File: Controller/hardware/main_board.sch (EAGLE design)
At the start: 45 parts, among them IC1 LINEAR_7805DT, IC2 40XX_4050D, IC3 ADAFRUIT_LP298XS, IC5 ATMEGA328, Q4 16MHZ, X1 ADAFRUIT_MICROSD, X4 CON-PHOENIX-508_MST2V

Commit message: added part numbers, consolidated parts,  cleaned up board/schematic
added part numbers for capacitors, resistors, ic's and the main 12v connector.

cleaned up the board layout a little, mainly just straightening traces.

fixed the through hole 100uf cap footprint to reflect the bom part, 2mm leads 5mm body

made both leds the same part number.

removed the polarized caps from the sd card and replaced with smd 0805 ceramic caps.

cleaned up the schematic a little and added a frame
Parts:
- 12V: device main_board:SPARKFUN_LED0805 -> main_board:LED_RED_08050805
- ACT: value RED -> ACT; device main_board:ADAFRUIT_LEDCHIP-LED0805 -> main_board:LED_RED_08050805
- C1: device main_board:10UF_08050805 -> main_board:C10UF_08050805
- C10, C4, C6, C7, C9: device main_board:100UF_ECE3.5-8 -> main_board:C100UF_ECE3.5-8
- C12, C13: device main_board:16PF_08050805 -> main_board:C16PF_08050805
- C14, C2, C3, C5, C8: device main_board:100NF_08050805 -> main_board:C0.1UF_08050805
- IC1: value LINEAR_7805DT -> LINEAR_78DT; device main_board:LINEAR_7805DT -> main_board:LINEAR_78DT
- IC3: value ADAFRUIT_LP298XS -> LP298XS; device main_board:ADAFRUIT_LP298XS -> main_board:LP298XS
- IC5: device main_board:SPARKFUN_ATMEGA168 -> main_board:ATMEGA328P
- R1: value 1K -> 1.0k; device main_board:ADAFRUIT_R-US_R0805 -> main_board:R1.0K_0805R0805
- R10: value 330r -> 330; device main_board:ADAFRUIT_R-US_R0805 -> main_board:R330_0805R0805
- R2, R3: value 10K -> 10k; device main_board:ADAFRUIT_R-US_R0805 -> main_board:R10K_0805R0805
- R7: value 10K -> 10k; device main_board:SPARKFUN_RESISTOR -> main_board:R10K_0805R0805
- R9: value 2.2K -> 2.2k; device main_board:SPARKFUN_RESISTOR -> main_board:R2.2K_0805R0805
- SW_NEXT: device main_board:ADAFRUIT_SPST_TACT-EVQQ2 -> main_board:TACT_SW_EVQQ2-EVQQ2
- X1: value ADAFRUIT_MICROSD -> MICROSD_SMD; device main_board:ADAFRUIT_MICROSD -> main_board:MICROSD_SMD
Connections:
- net +3V3: now also C2.1
- net VCC: no longer C2.1
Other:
- moved on the sheet: 12V, ACT, C1, C10, C12, C13, C14, C2, C3, C4, C5, C6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

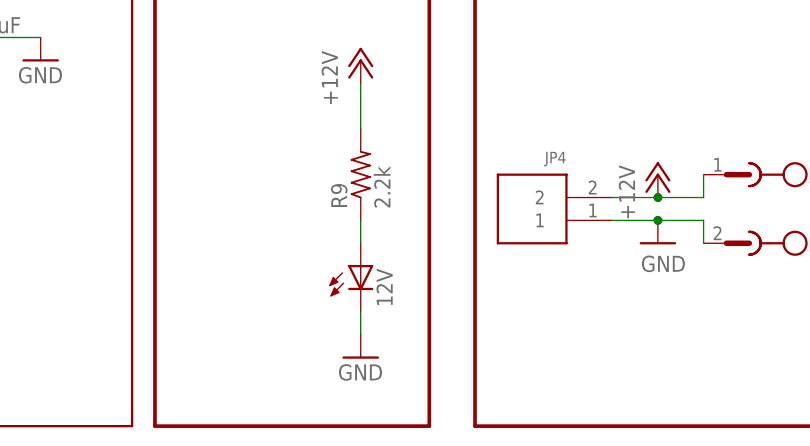
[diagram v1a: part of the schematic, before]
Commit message: final cleanup
little more silk screen shuffling and clearing DRC errors
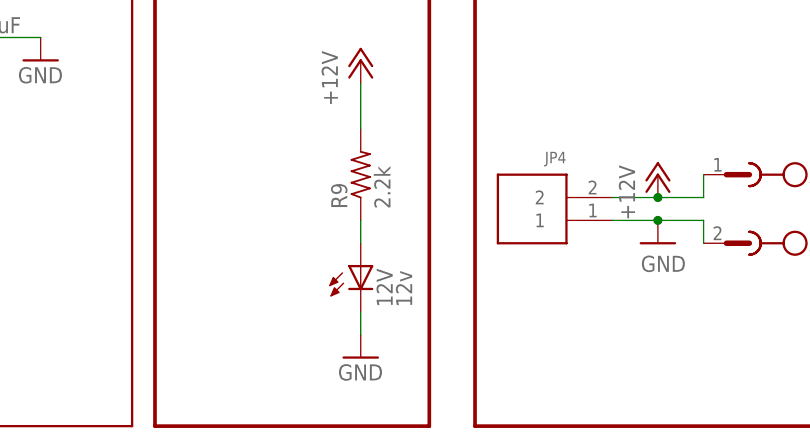
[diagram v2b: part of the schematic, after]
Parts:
- 12V: value (none) -> 12v
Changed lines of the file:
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@@
 <part name="P+18" library="main_board" deviceset="VCC" device=""/>
 <part name="R9" library="main_board" deviceset="R2.2K_0805" device="R0805" value="2.2k"/>
-<part name="12V" library="main_board" deviceset="LED_RED_0805" device="0805"/>
+<part name="12V" library="main_board" deviceset="LED_RED_0805" device="0805" value="12v"/>
 <part name="P+17" library="main_board" deviceset="+12V" device=""/>
 <part name="C8" library="main_board" deviceset="C0.1UF_0805" device="0805" value="0.1uF"/>
@@
 </sheet>
 </sheets>
-<errors>
-</errors>
 </schematic>
 </drawing>

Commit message: updated board name
changed board name to reflect copper changes
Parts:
- 12V: value 12v -> (none); device main_board:LED_RED_08050805 -> SparkFun:LED0805
- ACT: value ACT -> RED; device main_board:LED_RED_08050805 -> adafruit:LEDCHIP-LED0805
- C1: value 10uF -> 10uF/10V; device main_board:C10UF_08050805 -> adafruit:CPOL-USA/3216-18R
- C10, C4, C6, C7, C9: device main_board:C100UF_ECE3.5-8 -> rcl:CPOL-EUE3.5-8
- C12, C13: value 16pF -> 16pf; device main_board:C16PF_08050805 -> SparkFun:CAP0805
- C14, C3, C5, C8: value 0.1uF -> 100nF; device main_board:C0.1UF_08050805 -> SparkFun:CAP0805
- C2: device main_board:C0.1UF_08050805 -> adafruit:C-USC0805K
- IC1: value LINEAR_78DT -> 7805DT; device main_board:LINEAR_78DT -> linear:7805DT
- IC2: value 40XX_4050D -> 4050D; device main_board:40XX_4050D -> 40xx:4050D
- IC3: device main_board:LP298XS -> adafruit:LP298XS
- IC5: device main_board:ATMEGA328P -> SparkFun:ATMEGA168
- ICSP: device main_board:CON-HARTING-ML_ML6 -> con-harting-ml:ML6
- IC_A_MOTOR, IC_B_MOTOR: value POLOLU-STEPPER-DRIVER_2133-DRV8825 -> 2133-DRV8825; device main_board:POLOLU-STEPPER-DRIVER_2133-DRV8825 -> pololu-stepper-driver:2133-DRV8825
- J1: device main_board:JUMPER_J2X5MM -> jumper:J2X5MM
- JP1, JP5: device main_board:ADAFRUIT_PINHD-1X3 -> adafruit:PINHD-1X3
- JP4: value JST_EPH_2PIN -> 2PIN; device main_board:JST_EPH_2PIN -> jst_eph:2PIN
- MOTOR-A, MOTOR-B: value JST_EPH_4PIN -> 4PIN; device main_board:JST_EPH_4PIN -> jst_eph:4PIN
- Q4: device main_board:CRYSTAL_CRYSTALHC49S -> crystal:CRYSTALHC49S
- R1: value 1.0k -> 1K; device main_board:R1.0K_0805R0805 -> adafruit:R-US_R0805
- R10: value 330 -> 330r; device main_board:R330_0805R0805 -> adafruit:R-US_R0805
- R2, R3: value 10k -> 10K; device main_board:R10K_0805R0805 -> adafruit:R-US_R0805
- R7: value 10k -> 10K; device main_board:R10K_0805R0805 -> SparkFun:RESISTOR
- R9: value 2.2k -> 2.2K; device main_board:R2.2K_0805R0805 -> SparkFun:RESISTOR
- SJ1, SJ2, SJ3, SJ4, SJ5, SJ6: device main_board:JUMPER_SJ -> jumper:SJ
- SW_NEXT: device main_board:TACT_SW_EVQQ2-EVQQ2 -> adafruit:SPST_TACT-EVQQ2
- U$1: value DIY-MODULES_DISPLAY-OLED-128X64-I2C -> DISPLAY-OLED-128X64-I2C; device main_board:DIY-MODULES_DISPLAY-OLED-128X64-I2C -> diy-modules:DISPLAY-OLED-128X64-I2C
- X1: value MICROSD_SMD -> MICROSD; device main_board:MICROSD_SMD -> adafruit:MICROSD
- X4: value CON-PHOENIX-508_MST2V -> MST2V; device main_board:CON-PHOENIX-508_MST2V -> con-phoenix-508:MST2V
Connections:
- net +3V3: now also C1.+; no longer C1.1, C2.1
- net GND: now also C1.-; no longer C1.2
- net VCC: now also C2.1
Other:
- moved on the sheet: 12V, ACT, C10, C12, C13, C14, C2, C3, C4, C5, C6, C7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

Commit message: bom and silkscreen updates
bom information added to all the parts and the silkscreen was all normalized to 40mils and placed so there is no more overlapping. a few designators were missing from the board so i brought them back. the only copper change was c1. the old footprint didn't match the part used on the pdf bom.  i modified it to match the designated part.
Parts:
- 12V: device SparkFun:LED0805 -> main_board:LED_RED_08050805
- ACT: device adafruit:LEDCHIP-LED0805 -> main_board:LED_RED_08050805
- C1: value 10uF/10V -> 10uF; device adafruit:CPOL-USA/3216-18R -> main_board:C10UF_08050805
- C10, C4, C6, C7, C9: device rcl:CPOL-EUE3.5-8 -> main_board:RCL_CPOL-EUE3.5-8
- C12, C13: value 16pf -> 16pF; device SparkFun:CAP0805 -> main_board:C16PF_08050805
- C14, C3, C5, C8: value 100nF -> 0.1uF; device SparkFun:CAP0805 -> main_board:C0.1UF_08050805
- C2: device adafruit:C-USC0805K -> main_board:C0.1UF_08050805
- IC1: value 7805DT -> LINEAR_78DT; device linear:7805DT -> main_board:LINEAR_78DT
- IC2: value 4050D -> 40XX_4050D; device 40xx:4050D -> main_board:40XX_4050D
- IC3: device adafruit:LP298XS -> main_board:LP298XS
- IC5: device SparkFun:ATMEGA168 -> main_board:ATMEGA328P
- IC_A_MOTOR, IC_B_MOTOR: value 2133-DRV8825 -> POLOLU-STEPPER-DRIVER_2133-DRV8825; device pololu-stepper-driver:2133-DRV8825 -> main_board:POLOLU-STEPPER-DRIVER_2133-DRV8825
- J1: device jumper:J2X5MM -> main_board:JUMPER_J2X5MM
- Q4: device crystal:CRYSTALHC49S -> main_board:CRYSTAL_CRYSTALHC49S
- R1: value 1K -> 1.0k; device adafruit:R-US_R0805 -> main_board:R1.0K_0805R0805
- R10: value 330r -> 330; device adafruit:R-US_R0805 -> main_board:R330_0805R0805
- R2, R3: value 10K -> 10k; device adafruit:R-US_R0805 -> main_board:R10K_0805R0805
- R7: value 10K -> 10k; device SparkFun:RESISTOR -> main_board:R10K_0805R0805
- R9: value 2.2K -> 2.2k; device SparkFun:RESISTOR -> main_board:R2.2K_0805R0805
- SW_NEXT: device adafruit:SPST_TACT-EVQQ2 -> main_board:TACT_SW_EVQQ2-EVQQ2
- U$1: value DISPLAY-OLED-128X64-I2C -> DIY-MODULES_DISPLAY-OLED-128X64-I2C; device diy-modules:DISPLAY-OLED-128X64-I2C -> main_board:DIY-MODULES_DISPLAY-OLED-128X64-I2C
- X1: value MICROSD -> MICROSD_SMD; device adafruit:MICROSD -> main_board:MICROSD_SMD
- X4: value MST2V -> CON-PHOENIX-508_MST2V; device con-phoenix-508:MST2V -> main_board:CON-PHOENIX-508_MST2V
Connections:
- net +3V3: now also C1.1; no longer C1.+
- net GND: now also C1.2; no longer C1.-
